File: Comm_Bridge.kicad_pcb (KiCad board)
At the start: 2 copper layers, 66 x 55.9 mm, 98 parts, among them P1 USB_B, P2 CONN_01X03, P3 Solenoid, P4 XT60, P5 CONN_01X03, P6 CONN_01X03, U1 FT4232H, U10 ADM3251E, U11 ADM3251E, U2 93LC56BT-I/OT, U3 74HC595_CUST, U4 LM1117-XX, U5 ADC101S021, U6 NLSX4373, U7 NLSX4373, U8 ACPL-247-500E, U9 ACPL-247-500E, Y1 12MHz

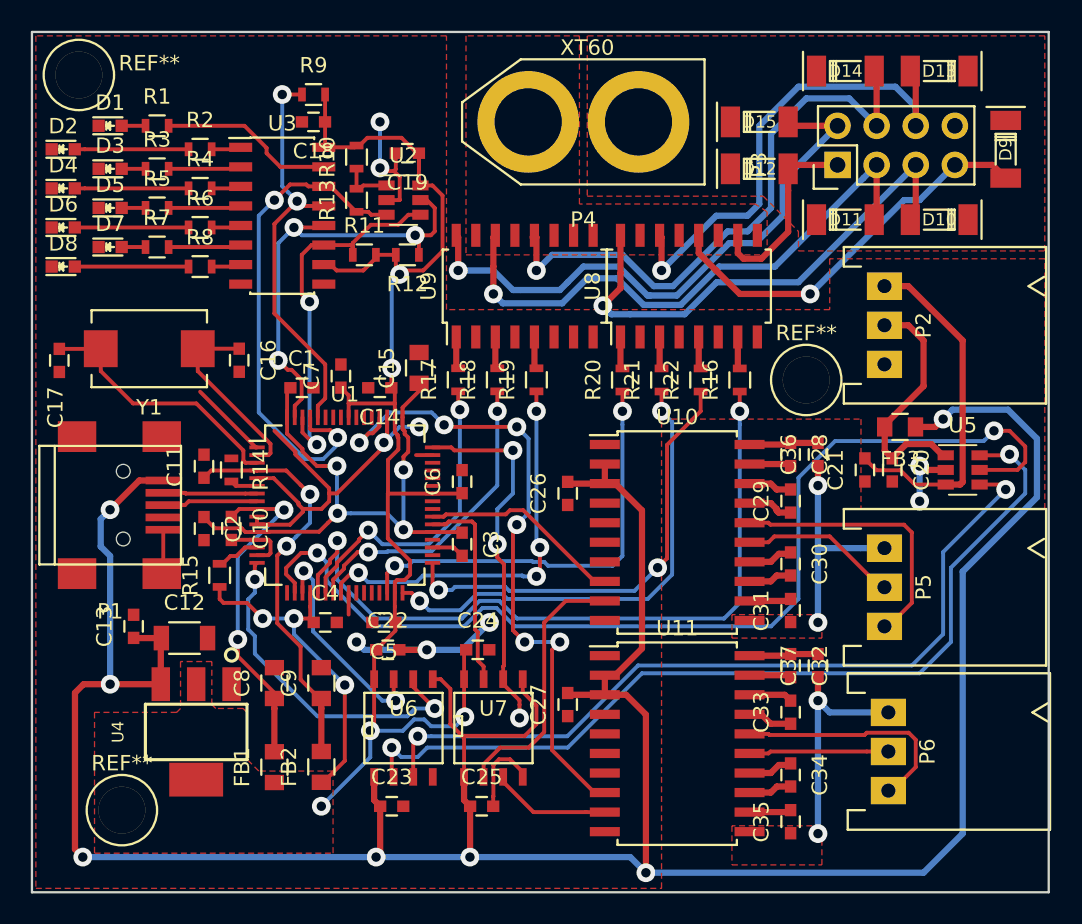
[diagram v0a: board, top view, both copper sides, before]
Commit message: Squashed 'Circuit/Peripheral_bridge/' changes from 4ec07b4..2bd5584
2bd5584 Update README.md
9c7d862 Merge branch 'Peripheral_Bridge'
ba635c8 Add footprint path as the new version of KiCad (4.0.6) refuses to search footprints in the schematic library search path.
b987a79 Add footprint path as the new version of KiCad (4.0.6) refuses to search footprints in the schematic library search path.
67c1d6b Change the version of KiCad to 4.0.6 and un-connected ID_Pin of the USB connector.
4150c41 Change the PCB footprints of C4.7uF and 3.3uF from 1206 to 0803 (smaller)
e412060 Merge branch 'Peripheral_Bridge_PCB_AjPong' into Peripheral_Bridge
55cd72b Remove schematic file, which has a lot of bugs
c92a937 First full release of Peripheral Bridge with all bug-fixed in schematic and routed PCB.
2cb3571 Final commit before merging to the main line
d8eb200 Add EEPROM data-sheet
074595c Merge branch 'Peripheral_Bridge_AjPong' of https://github.com/Pongkemon01/Zeabus-Elec-2017 into Peripheral_Bridge_AjPong
5660cc0 Finished the schematic of the main circuit including adding some data-sheets
36c1e74 Merge branch 'Peripheral_Bridge_AjPong' of https://github.com/Pongkemon01/Zeabus-Elec-2017 into Peripheral_Bridge_AjPong
a07a6e5 Finished the schematic of the main circuit including adding some data-sheets
27840f3 Initialized with configured project file and empty related files.
db576ea Initialized with configured project file and empty related files.
0c67a1f Adding specification of the Peripheral bridge and Power distribution to their corresponding README.md
d76c4fe Adding specifications and data-sheets plus application notes for the Peripheral Bridge
REVERT: 4ec07b4 Change REF resistor from 10k to 12k 1%
REVERT: af5bbf3 Bug fixed at NLSX4373 (Level Shifter)
REVERT: 16479e9 Bug fixed at 74HC595
REVERT: cba8210 ADC bug fixed
REVERT: bc80c78 Generated Panel and Gerber files
REVERT: e51a901 Add footprint path as the new version of KiCad (4.0.6) refuses to search footprints in the schematic l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
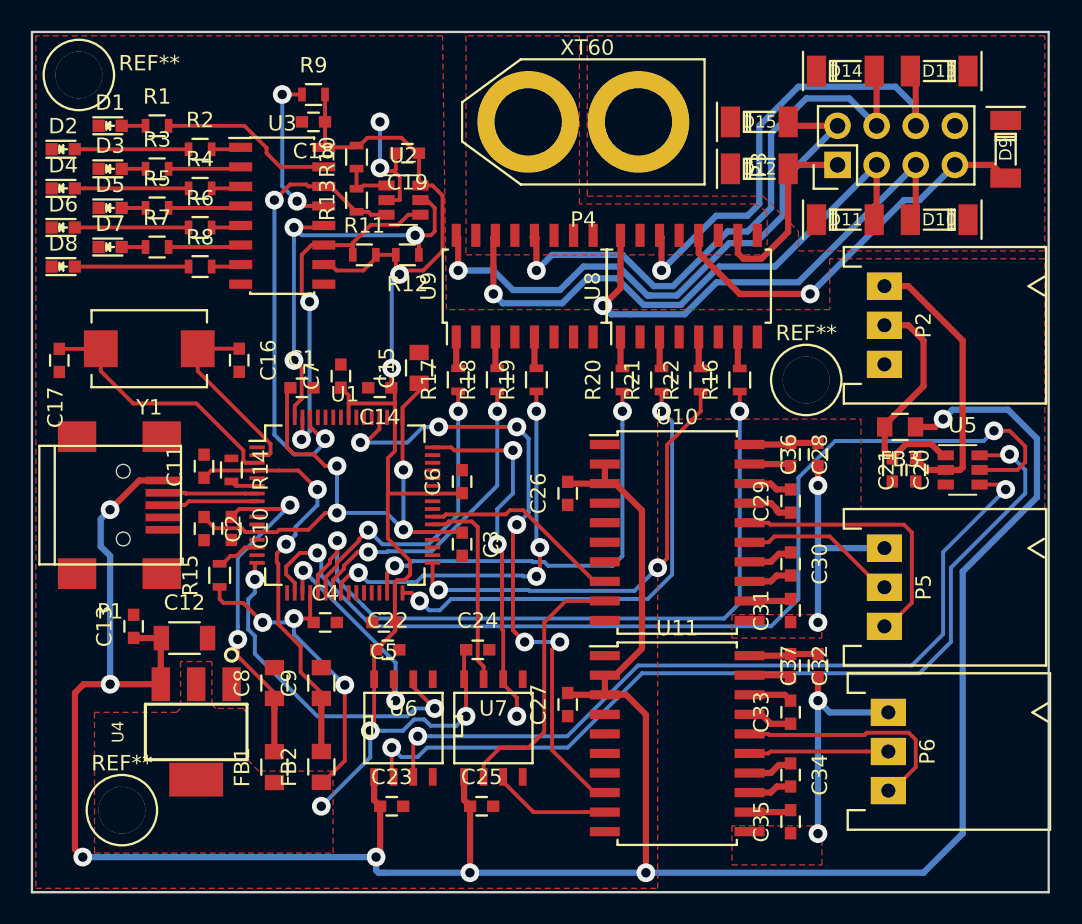
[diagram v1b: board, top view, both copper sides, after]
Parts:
- R14: value 12k 1% -> 10k
- moved C21 3.30 mm to (176.8, 104.6)
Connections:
- U1 pad 60: Net-(R9-Pad1) -> Net-(U1-Pad60)
- U5 pad 2: GND -> Net-(C21-Pad2)
- U5 pad 3: Net-(C21-Pad2) -> GND
- U6 pad 5: VBUS -> GND
- U7 pad 5: VBUS -> GND
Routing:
- net GND: track 73.3 -> 8.38 mm, vias 9 -> 2
- net Net-(R9-Pad1): track 26.7 -> 10.5 mm
- net VBUS: track 196.3 -> 181.5 mm
- net Net-(C21-Pad2): track 22.9 -> 18.2 mm
- net Net-(R13-Pad1): track 32.7 -> 30.1 mm
- net Net-(R12-Pad1): track 29.6 -> 28.2 mm
- net Net-(R11-Pad1): track 24.5 -> 23.4 mm
- net Net-(R16-Pad1): track 48.8 -> 47.8 mm
- net Net-(U1-Pad18): track 68.4 -> 67.5 mm
- net Net-(C10-Pad1): track 21.6 -> 22.5 mm
- net Net-(U1-Pad52): track 42.9 -> 42.0 mm
- net Net-(C11-Pad1): track 26.6 -> 27.4 mm
